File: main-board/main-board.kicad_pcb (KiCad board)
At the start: 2 copper layers, 100.1 x 67.1 mm, 50 parts, among them J1 Conn_02x08_Odd_Even, J2 7-12V, Q1 AO3400A, Q2 AO3400A, Q3 AO3400A, Q4 AO3400A, Q5 AO3400A, Q6 AO3400A, Q7 AO3400A, Q8 AO3400A, U1 40106, U2 4024, U3 4040, U4 27C256, U5 LM78L05, U6 ULN2803A, U7 4028, U9 L7805

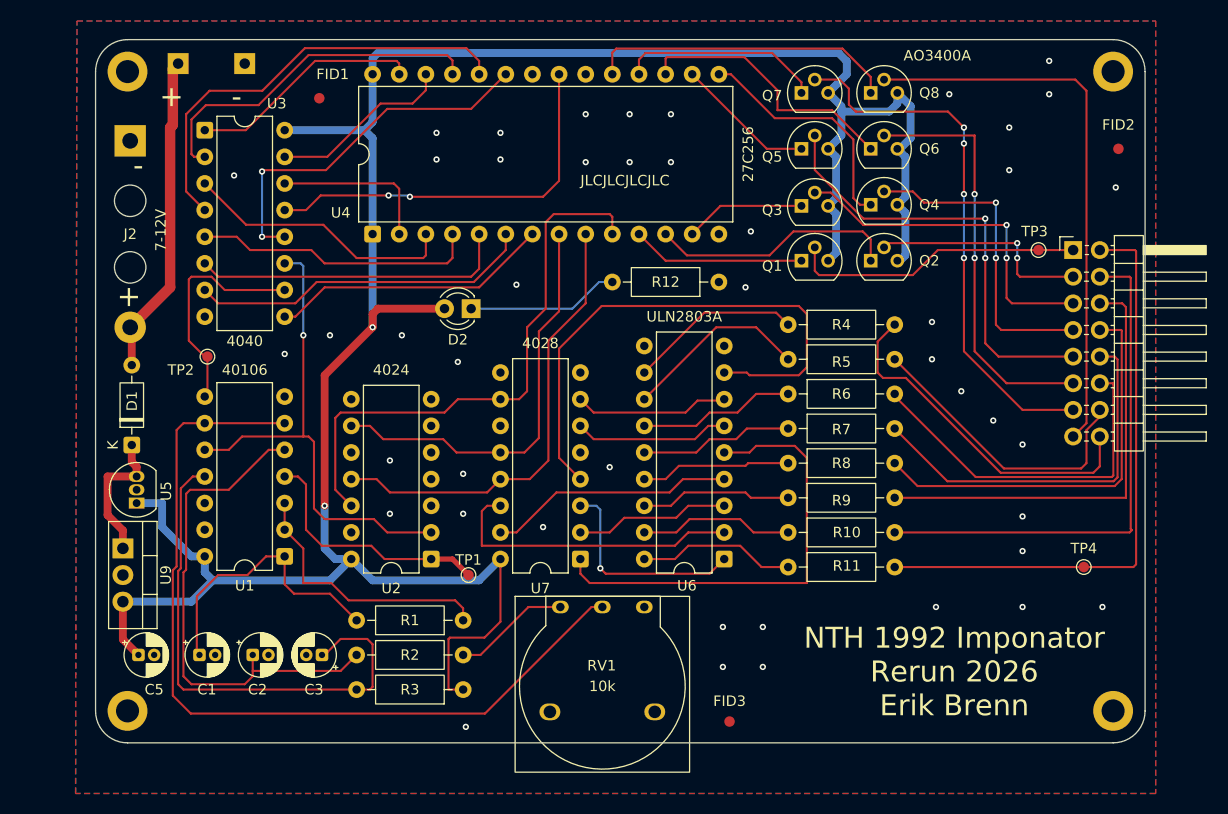
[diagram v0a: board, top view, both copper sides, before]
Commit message: fixed 2n7000 footprint and added testpoints
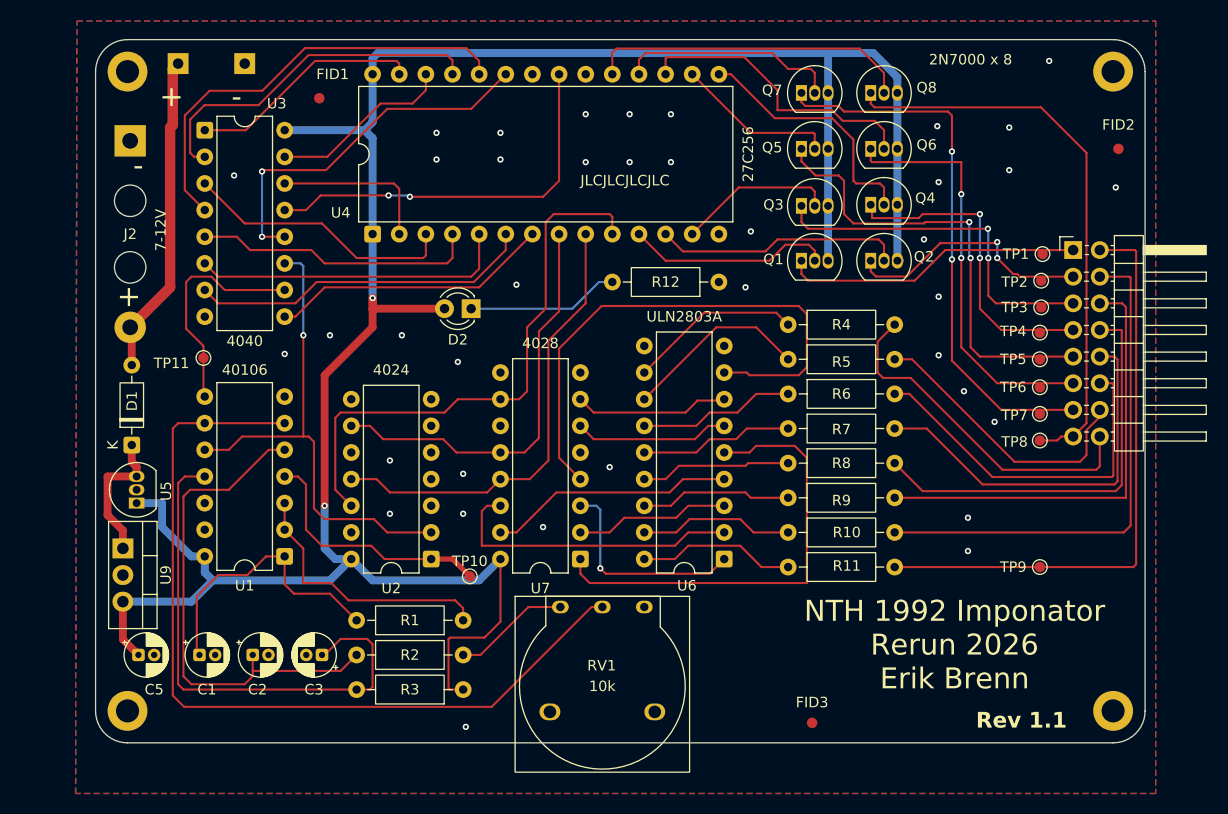
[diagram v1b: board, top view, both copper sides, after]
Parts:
- added TP10: TestPoint, ezee-footprints:TestPoint_Pad_D1.0mm, F.Cu at (135.3, 108.8)
- added TP11: TestPoint, ezee-footprints:TestPoint_Pad_D1.0mm, F.Cu at (109.9, 88.0)
- added TP5: TestPoint, ezee-footprints:TestPoint_Pad_D1.0mm, F.Cu at (189.6, 88.1)
- added TP6: TestPoint, ezee-footprints:TestPoint_Pad_D1.0mm, F.Cu at (189.6, 90.8)
- added TP7: TestPoint, ezee-footprints:TestPoint_Pad_D1.0mm, F.Cu at (189.6, 93.3)
- added TP8: TestPoint, ezee-footprints:TestPoint_Pad_D1.0mm, F.Cu at (189.6, 95.9)
- added TP9: TestPoint, ezee-footprints:TestPoint_Pad_D1.0mm, F.Cu at (189.6, 108.0)
- C1, C5: value 0.1u -> 0.22u
- Q1, Q2, Q3, Q4, Q5, Q6, Q7, Q8: value AO3400A -> 2N7000; footprint Package_TO_SOT_THT:TO-92 -> Package_TO_SOT_THT:TO-92_Inline
- R1: value 8.2k -> 12k
- R10, R11, R4, R5, R6, R7, R8, R9: value 330 -> 360
- moved TP2 79.8 mm to (189.7, 80.6)
- moved TP1 62.7 mm to (189.9, 78.1)
- moved TP4 22.7 mm to (189.6, 85.6)
- moved FID3 7.88 mm to (167.9, 122.8)
- moved TP3 5.47 mm to (189.7, 83.2)
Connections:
- Q1 pad 1: Net-(Q1-G) -> Net-(J1-Pin_1)
- Q1 pad 2: Net-(J1-Pin_1) -> Net-(Q1-G)
- Q2 pad 1: Net-(Q2-G) -> Net-(J1-Pin_3)
- Q2 pad 2: Net-(J1-Pin_3) -> Net-(Q2-G)
- Q3 pad 1: Net-(Q3-G) -> Net-(J1-Pin_5)
- Q3 pad 2: Net-(J1-Pin_5) -> Net-(Q3-G)
- Q4 pad 1: Net-(Q4-G) -> Net-(J1-Pin_7)
- Q4 pad 2: Net-(J1-Pin_7) -> Net-(Q4-G)
- Q5 pad 1: Net-(Q5-G) -> Net-(J1-Pin_9)
- Q5 pad 2: Net-(J1-Pin_9) -> Net-(Q5-G)
- Q6 pad 1: Net-(Q6-G) -> Net-(J1-Pin_11)
- Q6 pad 2: Net-(J1-Pin_11) -> Net-(Q6-G)
- Q7 pad 1: Net-(Q7-G) -> Net-(J1-Pin_13)
- Q7 pad 2: Net-(J1-Pin_13) -> Net-(Q7-G)
- Q8 pad 1: Net-(Q8-G) -> Net-(J1-Pin_15)
- Q8 pad 2: Net-(J1-Pin_15) -> Net-(Q8-G)
- TP1 pad 1: Net-(U2-~{CLK}) -> Net-(J1-Pin_1)
- TP2 pad 1: Net-(U3-CLK) -> Net-(J1-Pin_3)
- TP3 pad 1: Net-(J1-Pin_1) -> Net-(J1-Pin_5)
- TP4 pad 1: Net-(J1-Pin_2) -> Net-(J1-Pin_7)
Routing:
- net +5V: track 236.7 -> 232.1 mm
- net Net-(Q3-G): track 11.5 -> 15.1 mm
- net Net-(Q1-G): track 16.5 -> 19.6 mm
- net Net-(J1-Pin_3): track 21.3 -> 24.1 mm
- net Net-(Q6-G): track 25.9 -> 28.2 mm
- net Net-(Q5-G): track 13.4 -> 15.4 mm
- net Net-(Q7-G): track 19.3 -> 21.1 mm
- net Net-(J1-Pin_13): track 51.1 -> 52.6 mm, vias 4 -> 2
- net Net-(Q8-G): track 29.5 -> 31.0 mm
- net Net-(J1-Pin_9): track 42.3 -> 43.7 mm
- net Net-(Q4-G): track 22.9 -> 24.2 mm
- net Net-(J1-Pin_15): track 53.2 -> 54.4 mm
- net Net-(J1-Pin_14): track 28.4 -> 27.4 mm
- net Net-(J1-Pin_5): track 33.1 -> 34.0 mm
- net Net-(J1-Pin_8): track 39.1 -> 39.8 mm
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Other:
- board text added: "2N7000 x 8"
- board text added: "Rev 1.1"

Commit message: Started migrating to SMD
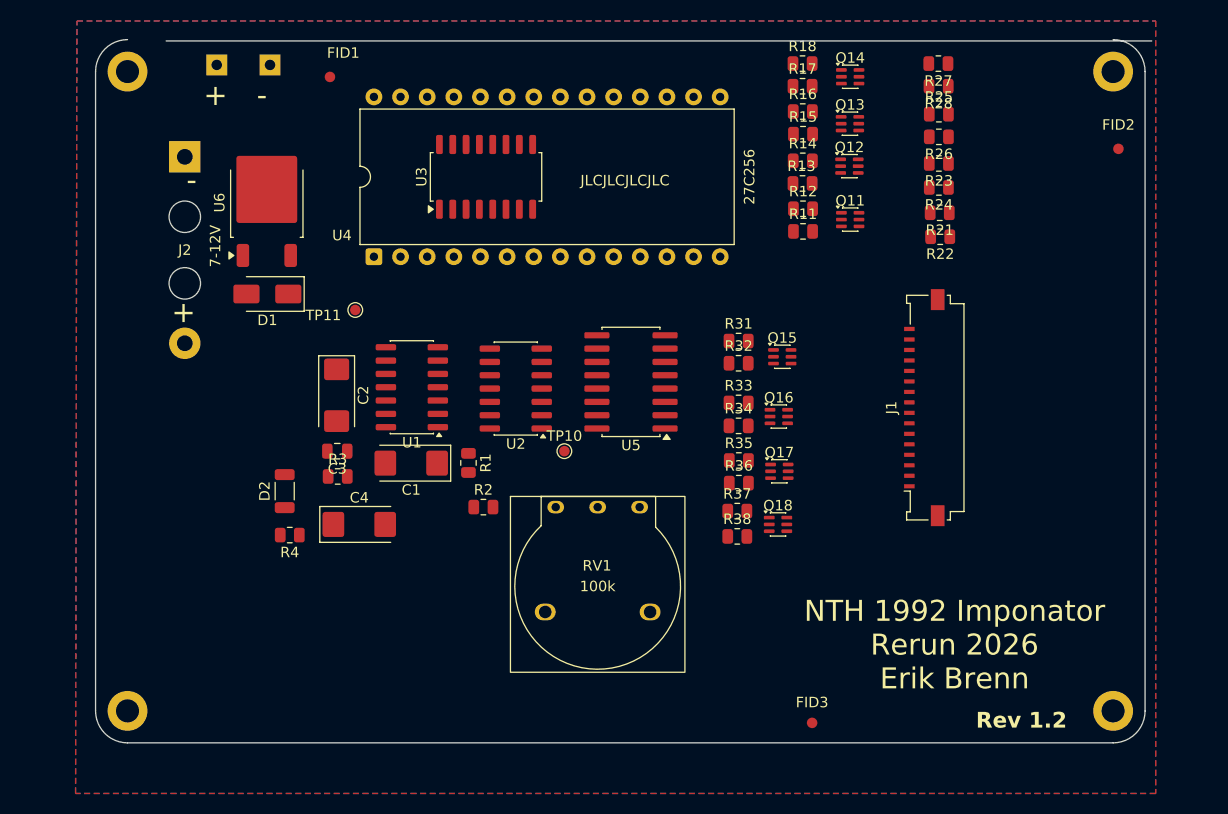
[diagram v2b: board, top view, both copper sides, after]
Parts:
- removed C5: 0.22u, Capacitor_THT:CP_Radial_D4.0mm_P1.50mm
- removed Q1, Q2, Q3, Q4, Q5, Q6, Q7, Q8: 2N7000, Package_TO_SOT_THT:TO-92_Inline
- removed R10, R5, R6, R7, R8, R9: 360, Resistor_THT:R_Axial_DIN0207_L6.3mm_D2.5mm_P10.16mm_Horizontal
- removed TP1, TP2, TP3, TP4, TP5, TP6, TP7, TP8, TP9: TestPoint, ezee-footprints:TestPoint_Pad_D1.0mm
- removed U7: 4028, Package_DIP:DIP-16_W7.62mm
- removed U9: L7805, Package_TO_SOT_THT:TO-220-3_Vertical
- added C4: 4.7u, Capacitor_Tantalum_SMD:CP_EIA-6032-15_Kemet-U, F.Cu at (124.7, 103.9)
- added Q11: MBT3904DW1, Package_TO_SOT_SMD:SOT-363_SC-70-6, F.Cu at (171.5, 74.8)
- added Q12: MBT3904DW1, Package_TO_SOT_SMD:SOT-363_SC-70-6, F.Cu at (171.4, 69.7)
- added Q13: MBT3904DW1, Package_TO_SOT_SMD:SOT-363_SC-70-6, F.Cu at (171.5, 65.7)
- added Q14: MBT3904DW1, Package_TO_SOT_SMD:SOT-363_SC-70-6, F.Cu at (171.5, 61.2)
- added Q15: MBT3904DW1, Package_TO_SOT_SMD:SOT-363_SC-70-6, F.Cu at (165.0, 87.9)
- added Q16: MBT3904DW1, Package_TO_SOT_SMD:SOT-363_SC-70-6, F.Cu at (164.7, 93.6)
- added Q17: MBT3904DW1, Package_TO_SOT_SMD:SOT-363_SC-70-6, F.Cu at (164.8, 98.8)
- added Q18: MBT3904DW1, Package_TO_SOT_SMD:SOT-363_SC-70-6, F.Cu at (164.6, 103.9)
- added R13: 8.2k, Resistor_SMD:R_0805_2012Metric, F.Cu at (167.0, 71.4)
- added R14: 8.2k, Resistor_SMD:R_0805_2012Metric, F.Cu at (167.0, 69.2)
- added R15: 8.2k, Resistor_SMD:R_0805_2012Metric, F.Cu at (167.0, 66.7)
- added R16: 8.2k, Resistor_SMD:R_0805_2012Metric, F.Cu at (167.0, 64.5)
- added R17: 8.2k, Resistor_SMD:R_0805_2012Metric, F.Cu at (167.0, 62.1)
- added R18: 8.2k, Resistor_SMD:R_0805_2012Metric, F.Cu at (167.0, 59.9)
- added R21: 120, Resistor_SMD:R_0805_2012Metric, F.Cu at (180.1, 74.2)
- added R22: 120, Resistor_SMD:R_0805_2012Metric, F.Cu at (180.1, 76.5)
- added R23: 120, Resistor_SMD:R_0805_2012Metric, F.Cu at (180.0, 69.5)
- added R24: 120, Resistor_SMD:R_0805_2012Metric, F.Cu at (180.0, 71.8)
- added R25: 120, Resistor_SMD:R_0805_2012Metric, F.Cu at (180.0, 64.8)
- added R26: 120, Resistor_SMD:R_0805_2012Metric, F.Cu at (180.0, 66.9)
- added R27: 120, Resistor_SMD:R_0805_2012Metric, F.Cu at (179.9, 59.9)
- added R28: 120, Resistor_SMD:R_0805_2012Metric, F.Cu at (180.0, 62.1)
- added R31: 2.7k, Resistor_SMD:R_0805_2012Metric, F.Cu at (160.9, 86.4)
- added R32: 2.7k, Resistor_SMD:R_0805_2012Metric, F.Cu at (160.9, 88.5)
- added R33: 2.7k, Resistor_SMD:R_0805_2012Metric, F.Cu at (160.9, 92.3)
- added R34: 2.7k, Resistor_SMD:R_0805_2012Metric, F.Cu at (160.9, 94.5)
- added R35: 2.7k, Resistor_SMD:R_0805_2012Metric, F.Cu at (160.9, 97.8)
- added R36: 2.7k, Resistor_SMD:R_0805_2012Metric, F.Cu at (160.9, 99.9)
- added R37: 2.7k, Resistor_SMD:R_0805_2012Metric, F.Cu at (160.8, 102.6)
- added R38: 2.7k, Resistor_SMD:R_0805_2012Metric, F.Cu at (160.8, 105.0)
- C1: value 0.22u -> 1u; footprint Capacitor_THT:CP_Radial_D4.0mm_P1.50mm -> Capacitor_Tantalum_SMD:CP_EIA-6032-15_Kemet-U
- C2: value 10u -> 4.7u; footprint Capacitor_THT:CP_Radial_D4.0mm_P1.50mm -> Capacitor_Tantalum_SMD:CP_EIA-6032-15_Kemet-U
- C3: value 0.1u -> 390n; footprint Capacitor_THT:CP_Radial_D4.0mm_P1.50mm -> Capacitor_SMD:C_0805_2012Metric
- D1: value 1N4148 -> SS12; footprint Diode_THT:D_DO-35_SOD27_P7.62mm_Horizontal -> Diode_SMD:D_SMA
- D2: footprint LED_THT:LED_D3.0mm -> Inductor_SMD:L_1206_3216Metric
- J1: value Conn_02x08_Odd_Even -> 16-bit; footprint Connector_PinHeader_2.54mm:PinHeader_2x08_P2.54mm_Horizontal -> Connector_FFC-FPC:Molex_200528-0160_1x16-1MP_P1.00mm_Horizontal
- R1: value 12k -> 470; footprint Resistor_THT:R_Axial_DIN0207_L6.3mm_D2.5mm_P10.16mm_Horizontal -> Resistor_SMD:R_0805_2012Metric
- R11, R12: value 360 -> 8.2k; footprint Resistor_THT:R_Axial_DIN0207_L6.3mm_D2.5mm_P10.16mm_Horizontal -> Resistor_SMD:R_0805_2012Metric
- R2: value 5.6k -> 4.7k; footprint Resistor_THT:R_Axial_DIN0207_L6.3mm_D2.5mm_P10.16mm_Horizontal -> Resistor_SMD:R_0805_2012Metric
- R3: footprint Resistor_THT:R_Axial_DIN0207_L6.3mm_D2.5mm_P10.16mm_Horizontal -> Resistor_SMD:R_0805_2012Metric
- R4: value 360 -> 680; footprint Resistor_THT:R_Axial_DIN0207_L6.3mm_D2.5mm_P10.16mm_Horizontal -> Resistor_SMD:R_0805_2012Metric
- RV1: value 10k -> 100k
- U1: value 40106 -> CD40106BM96; footprint Package_DIP:DIP-14_W7.62mm -> Package_SO:SOIC-14_3.9x8.7mm_P1.27mm
- U2: value 4024 -> CD4024BM96; footprint Package_DIP:DIP-14_W7.62mm -> Package_SO:SOIC-14_3.9x8.7mm_P1.27mm
- U3: value 4040 -> CD4040BNSR; footprint Package_DIP:DIP-16_W7.62mm -> Package_SO:SOP-16_4.4x10.4mm_P1.27mm
- U5: value LM78L05 -> CD4028BM96; footprint Package_TO_SOT_THT:TO-92_Inline -> Package_SO:SOIC-16W_5.3x10.2mm_P1.27mm
- U6: value ULN2803A -> KA78M05_TO252; footprint Package_DIP:DIP-18_W7.62mm -> Package_TO_SOT_SMD:TO-252-2
- moved U6 55.3 mm to (115.9, 73.2), turned to 90 degrees
- moved R4 51.6 mm to (118.1, 104.9), turned to 180 degrees
- moved U5 48.5 mm to (150.6, 90.3), turned to 180 degrees
- moved R11 32.0 mm to (167.0, 75.9)
- moved C1 27.2 mm to (129.7, 98.0), turned to 180 degrees
- moved U3 27.2 mm to (136.8, 70.7), turned to 90 degrees
- moved C2 26.0 mm to (122.6, 91.6), turned to -90 degrees
- moved D2 24.9 mm to (117.6, 100.7), turned to 90 degrees
- moved R3 23.6 mm to (122.7, 99.3), turned to 0 degrees
- moved J1 21.0 mm to (178.1, 92.7), turned to 90 degrees
- moved U1 20.2 mm to (129.7, 90.8)
- moved C3 19.5 mm to (122.6, 96.9)
- moved D1 19.4 mm to (116.0, 81.9), turned to 180 degrees
- moved R2 18.6 mm to (136.5, 102.2)
- moved U2 18.1 mm to (139.6, 90.9)
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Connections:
- J1 pad 1: Net-(J1-Pin_1) -> O8
- J1 pad 10: Net-(J1-Pin_10) -> I7
- J1 pad 11: Net-(J1-Pin_11) -> I6
- J1 pad 12: Net-(J1-Pin_12) -> I5
- J1 pad 13: Net-(J1-Pin_13) -> I4
- J1 pad 14: Net-(J1-Pin_14) -> I3
- J1 pad 15: Net-(J1-Pin_15) -> I2
- J1 pad 16: Net-(J1-Pin_16) -> I1
- J1 pad 2: Net-(J1-Pin_2) -> O7
- J1 pad 3: Net-(J1-Pin_3) -> O6
- J1 pad 4: Net-(J1-Pin_4) -> O5
- J1 pad 5: Net-(J1-Pin_5) -> O4
- J1 pad 6: Net-(J1-Pin_6) -> 03
- J1 pad 7: Net-(J1-Pin_7) -> O2
- J1 pad 8: Net-(J1-Pin_8) -> O1
- J1 pad 9: Net-(J1-Pin_9) -> I8
- R11 pad 1: Net-(U6-O1) -> Net-(U4-D0)
- R11 pad 2: Net-(J1-Pin_2) -> Net-(Q11A-B1)
- R12 pad 1: GND -> Net-(U4-D1)
- R12 pad 2: Net-(D2-K) -> Net-(Q11B-B2)
- R4 pad 1: Net-(U6-O8) -> GND
- R4 pad 2: Net-(J1-Pin_16) -> Net-(D2-K)
- U4 pad 11: Net-(Q1-G) -> Net-(U4-D0)
- U4 pad 12: Net-(Q2-G) -> Net-(U4-D1)
- U5 pad 1: +5V -> Net-(U5-S4)
- U5 pad 2: GND -> Net-(U5-S2)
- U5 pad 3: Net-(D1-K) -> Net-(U5-S0)
- U6 pad 1: Net-(U6-I1) -> Net-(D1-K)
- U6 pad 2: Net-(U6-I2) -> GND
- U6 pad 3: Net-(U6-I3) -> +5V
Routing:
- net +5V: track 232.1 -> 0.00 mm, vias 2 -> 0
- net Net-(RV1-Pad2): track 81.7 -> 0.00 mm
- net Net-(J1-Pin_2): track 56.5 -> 0.00 mm
- net Net-(J1-Pin_15): track 54.4 -> 0.00 mm
- net Net-(U2-Q0): track 53.6 -> 0.00 mm
- net Net-(J1-Pin_13): track 52.6 -> 0.00 mm, vias 2 -> 0
- net Net-(U6-I8): track 52.3 -> 0.00 mm
- net Net-(C3-Pad1): track 50.6 -> 0.00 mm
- net Net-(J1-Pin_4): track 49.4 -> 0.00 mm
- net Net-(C2-Pad1): track 48.4 -> 0.00 mm
- net Net-(U2-MR): track 47.8 -> 0.00 mm, vias 1 -> 0
- net Net-(U6-I5): track 43.9 -> 0.00 mm
- net Net-(J1-Pin_9): track 43.7 -> 0.00 mm, vias 2 -> 0
- net Net-(U2-Q1): track 43.6 -> 0.00 mm
- net Net-(J1-Pin_6): track 42.9 -> 0.00 mm
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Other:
- board size 100.1 x 67.1 mm -> 100.7 x 67.1 mm
- board text added: "Rev 1.2"
- board text removed: "2N7000 x 8"
- board text removed: "Rev 1.1"

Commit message: routing complete - ready for QA
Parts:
- J2: footprint ezee-footprints:Battery_Terminals -> kicad-ezee-footprints:Battery_Terminals
- RV1: footprint ezee-footprints:Potentiometer_Wheel_3pin_Pitch4mm -> kicad-ezee-footprints:Potentiometer_Wheel_3pin_Pitch4mm
- TP10, TP11: footprint ezee-footprints:TestPoint_Pad_D1.0mm -> kicad-ezee-footprints:TestPoint_Pad_D1.0mm
- TPH1, TPH2: footprint ezee-footprints:TestPoint_Hook -> kicad-ezee-footprints:TestPoint_Hook
- moved FID1 65.4 mm to (187.2, 65.3)
- moved FID3 61.3 mm to (106.9, 116.3)
- moved FID2 45.3 mm to (186.2, 112.0)
- moved RV1 30.8 mm to (112.6, 100.7), turned to -90 degrees
- moved C4 29.6 mm to (108.4, 79.2), turned to 90 degrees
- moved U3 20.6 mm to (116.2, 72.0), turned to 0 degrees
- moved R2 19.6 mm to (117.2, 99.4), turned to -90 degrees
- moved U6 17.3 mm to (112.9, 90.2), turned to -90 degrees
- moved D1 15.6 mm to (103.8, 91.7)
- moved MH3 11.8 mm to (186.2, 116.1)
- moved MH4 10.4 mm to (186.2, 60.7)
- moved Q15 7.66 mm to (171.3, 83.4)
- moved Q16 7.66 mm to (170.9, 89.1)
- moved R35 7.66 mm to (167.1, 93.3)
- moved Q17 7.66 mm to (171.0, 94.4)
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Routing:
- net +5V: track 0.00 -> 186.7 mm, vias 0 -> 15
- net Net-(U2-MR): track 0.00 -> 73.3 mm
- net I7: track 0.00 -> 56.8 mm
- net I5: track 0.00 -> 49.8 mm
- net Net-(RV1-Pad2): track 0.00 -> 43.6 mm
- net Net-(C2-Pad1): track 0.00 -> 40.0 mm
- net I8: track 0.00 -> 39.1 mm
- net Net-(U2-Q1): track 0.00 -> 38.7 mm
- net Net-(U3-Q6): track 0.00 -> 37.1 mm
- net I3: track 0.00 -> 35.6 mm
- net Net-(U5-S7): track 0.00 -> 34.6 mm
- net Net-(D1-A): track 0.00 -> 34.3 mm
- net Net-(U3-Q1): track 0.00 -> 33.7 mm
- net I6: track 0.00 -> 32.0 mm
- net Net-(U3-Q7): track 0.00 -> 31.5 mm
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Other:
- board size 100.7 x 67.1 mm -> 89.8 x 61.6 mm
